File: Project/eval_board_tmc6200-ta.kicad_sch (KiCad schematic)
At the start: 0 parts

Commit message: Cleanup ED A1 version
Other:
- sheet BLDC_MOTOR.sch renamed BLDC_MOTOR
- sheet BUCK_Converter.sch renamed BUCK_Converter
- sheet IO Expander.sch renamed IO Expander
- sheet Microcontroller.sch renamed Microcontroller
- sheet IO Expander ports: added EXP_INT{A B}, I2C{SCK SDA}; removed EXP_INT_A, EXP_INT_B, I2C1_SCL, I2C1_SDA
- sheet Microcontroller ports: added EXP_INT{A B}, I2C{SCK SDA}; removed EXP_INT_A, EXP_INT_B, I2C1_SCL, I2C1_SDA

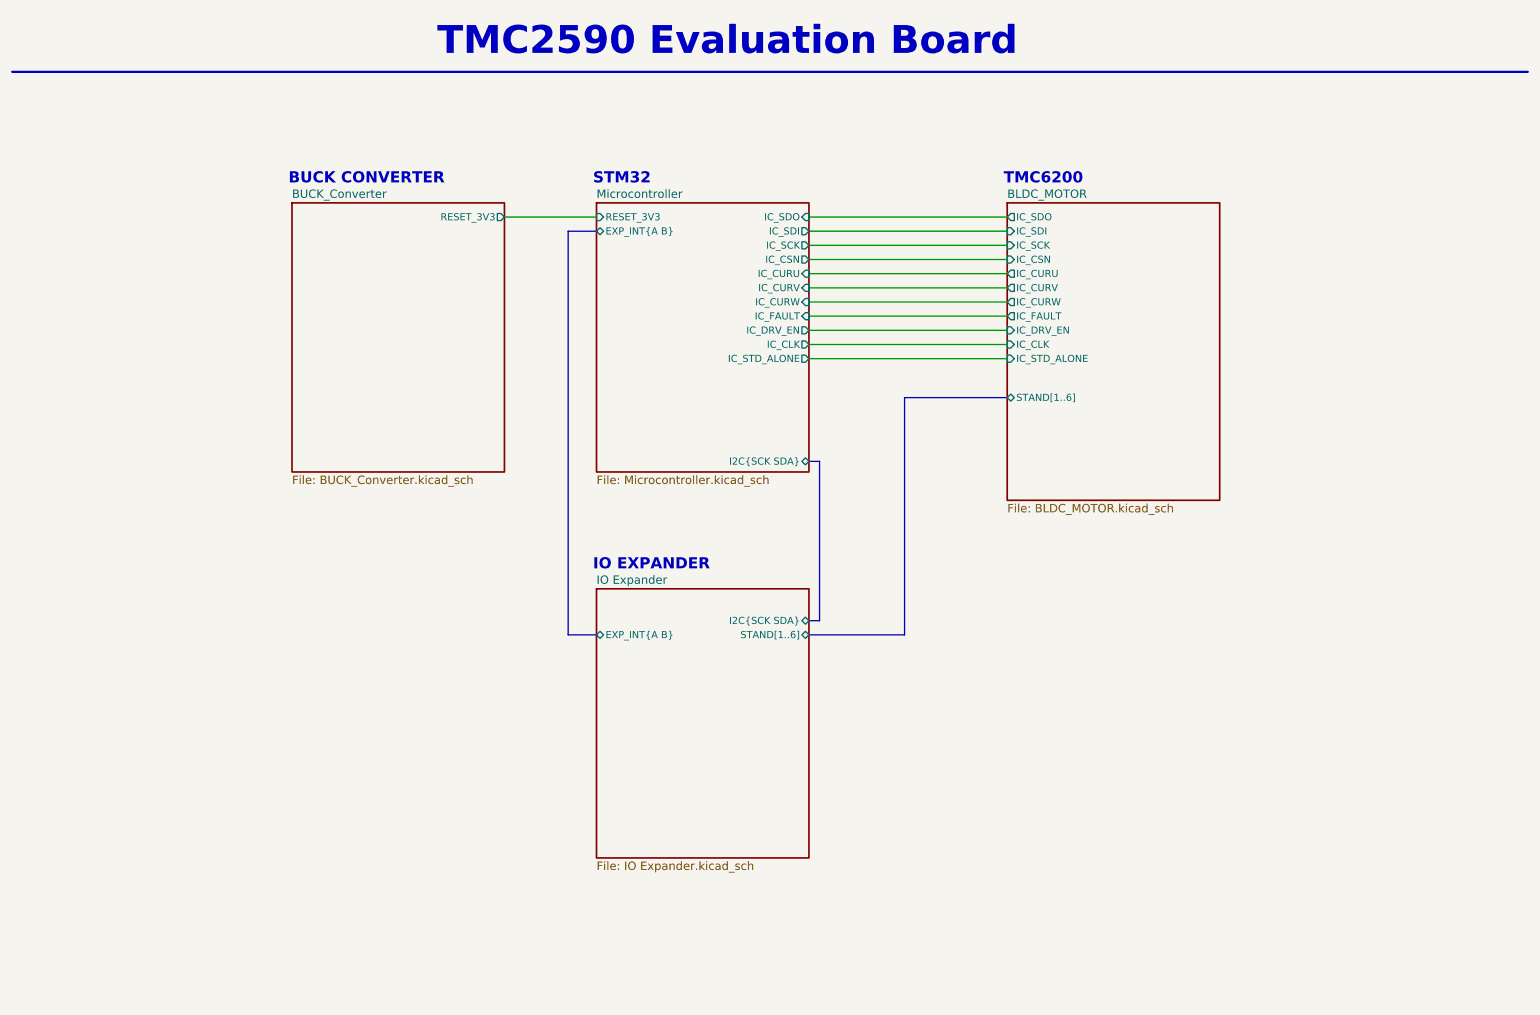
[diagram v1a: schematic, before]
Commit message: Cleaning files, added testpoints
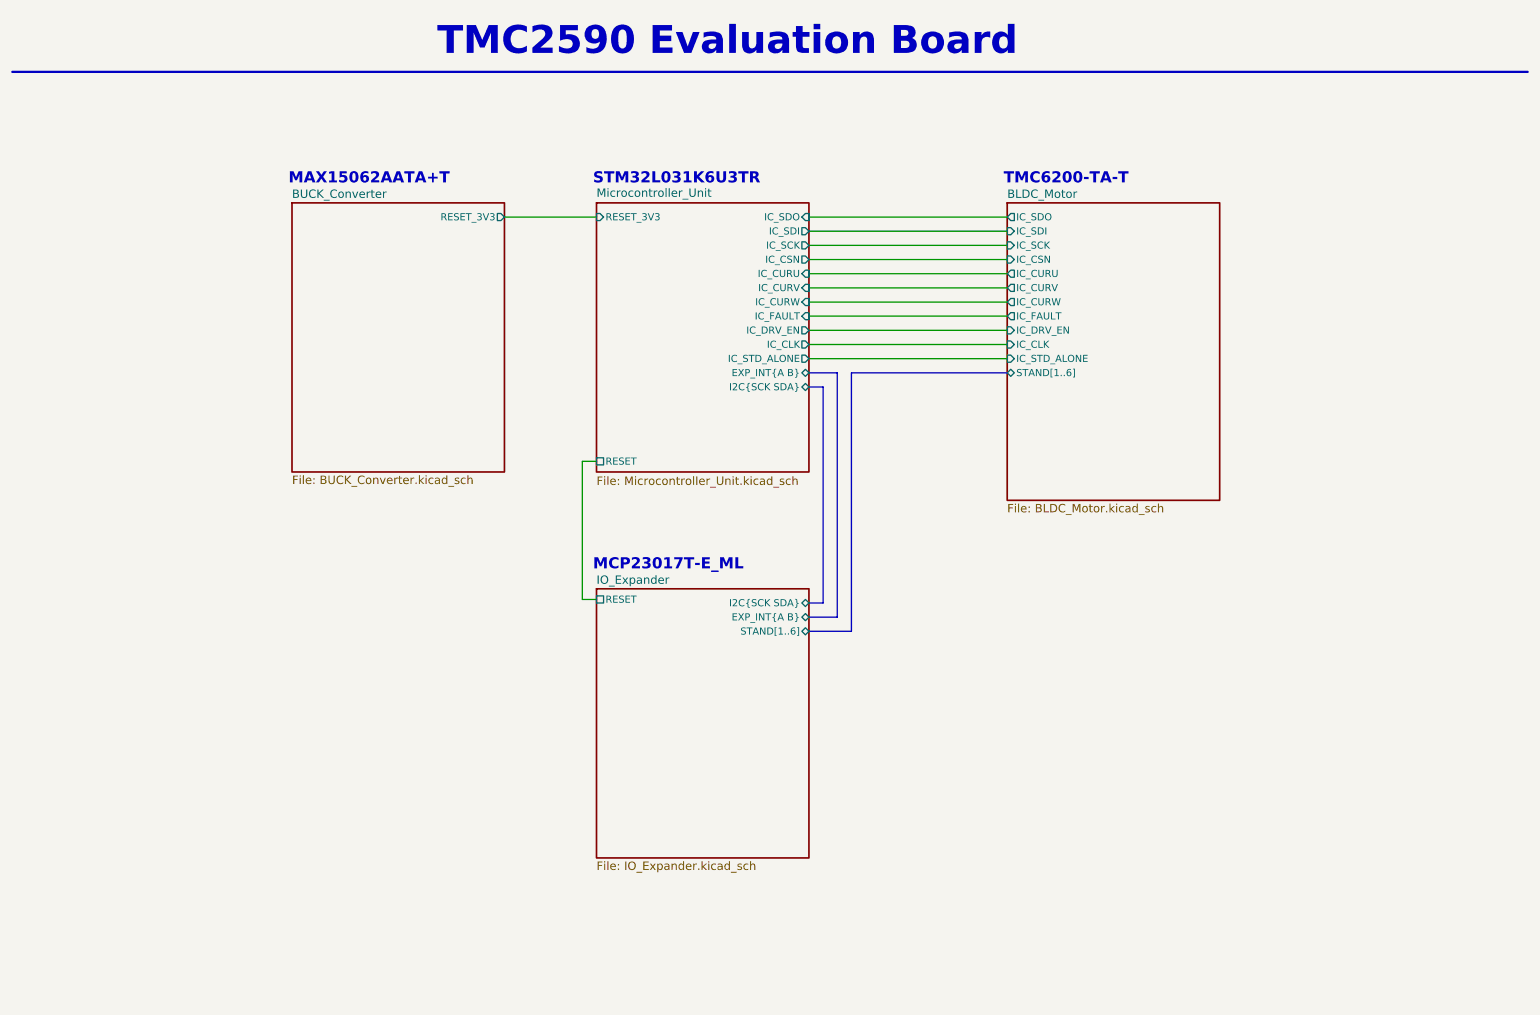
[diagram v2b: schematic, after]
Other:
- sheet BLDC_MOTOR renamed BLDC_Motor
- sheet IO Expander renamed IO_Expander
- sheet Microcontroller renamed Microcontroller_Unit
- sheet BLDC_Motor: file BLDC_MOTOR.kicad_sch -> BLDC_Motor.kicad_sch
- sheet IO_Expander: file IO Expander.kicad_sch -> IO_Expander.kicad_sch
- sheet IO_Expander ports: added RESET; removed none
- sheet Microcontroller_Unit: file Microcontroller.kicad_sch -> Microcontroller_Unit.kicad_sch
- sheet Microcontroller_Unit ports: added RESET; removed none
- note added: "MAX15062AATA+T"
- note added: "MCP23017T-E_ML"
- note added: "STM32L031K6U3TR"
- note added: "TMC6200-TA-T"
- note removed: "BUCK CONVERTER"
- note removed: "IO EXPANDER"
- note removed: "STM32"
- note removed: "TMC6200"
